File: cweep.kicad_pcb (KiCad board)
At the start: 2 copper layers, 106.6 x 82.7 mm, 51 parts

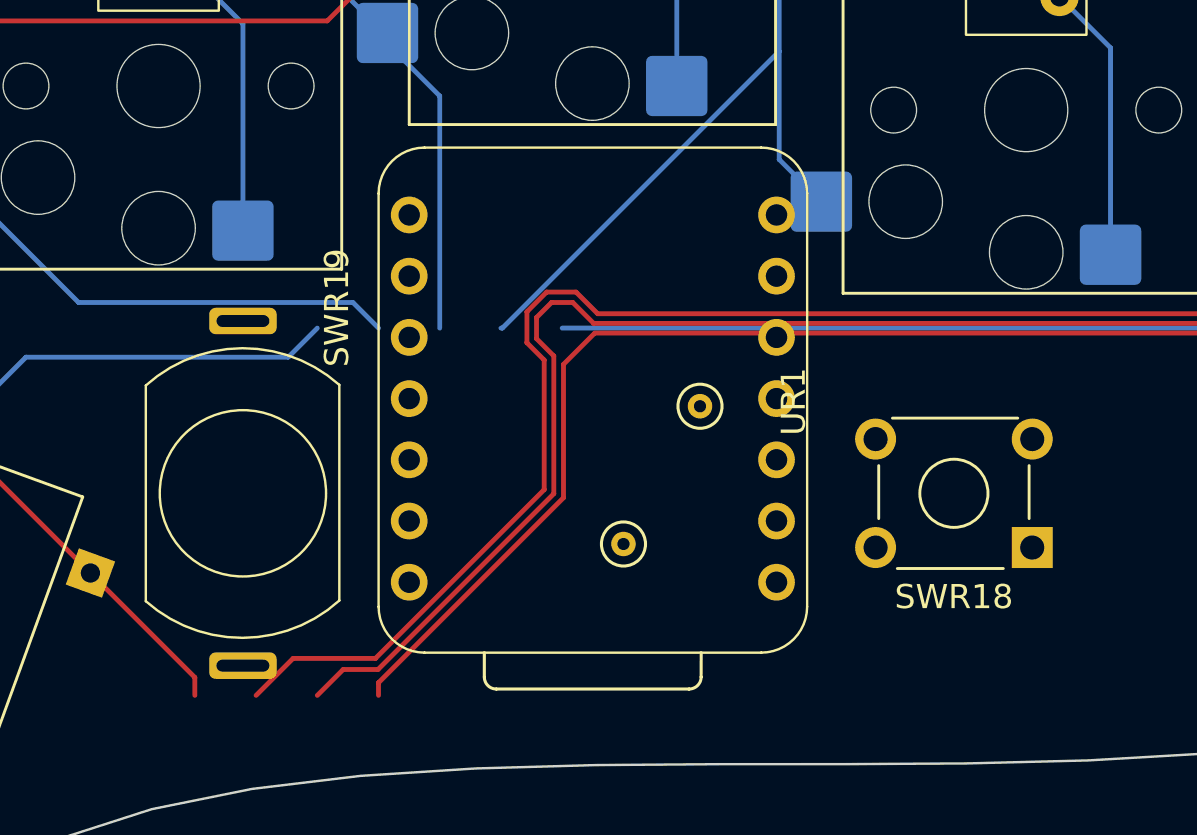
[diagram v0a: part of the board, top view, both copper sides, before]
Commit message: fix: align reset switch with power switch
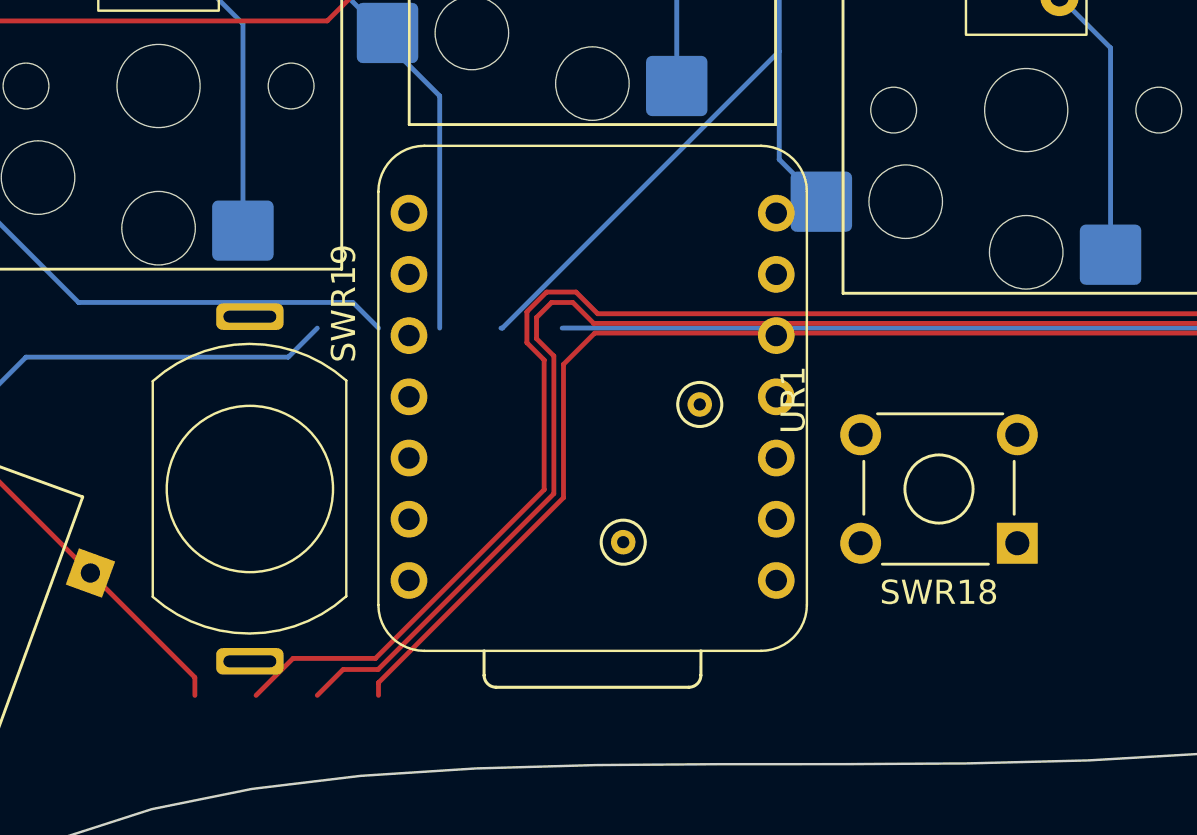
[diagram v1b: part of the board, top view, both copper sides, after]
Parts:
- moved SWR18 0.64 mm to (240.6, 102.0)
- moved SWR19 0.34 mm to (208.8, 99.7)
- moved UR1 0.07 mm to (222.9, 96.0)

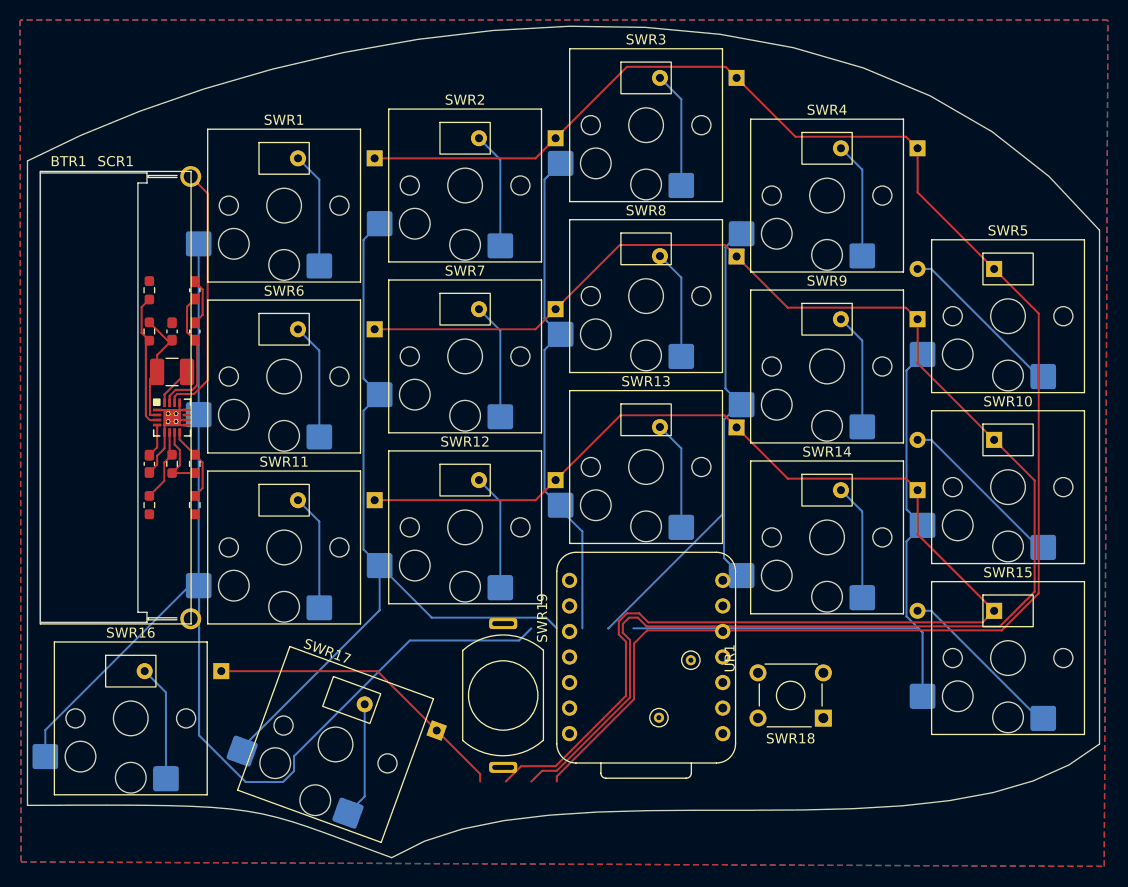
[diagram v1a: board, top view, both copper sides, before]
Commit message: fix: re-attach traces for gpio, power, and reset switches
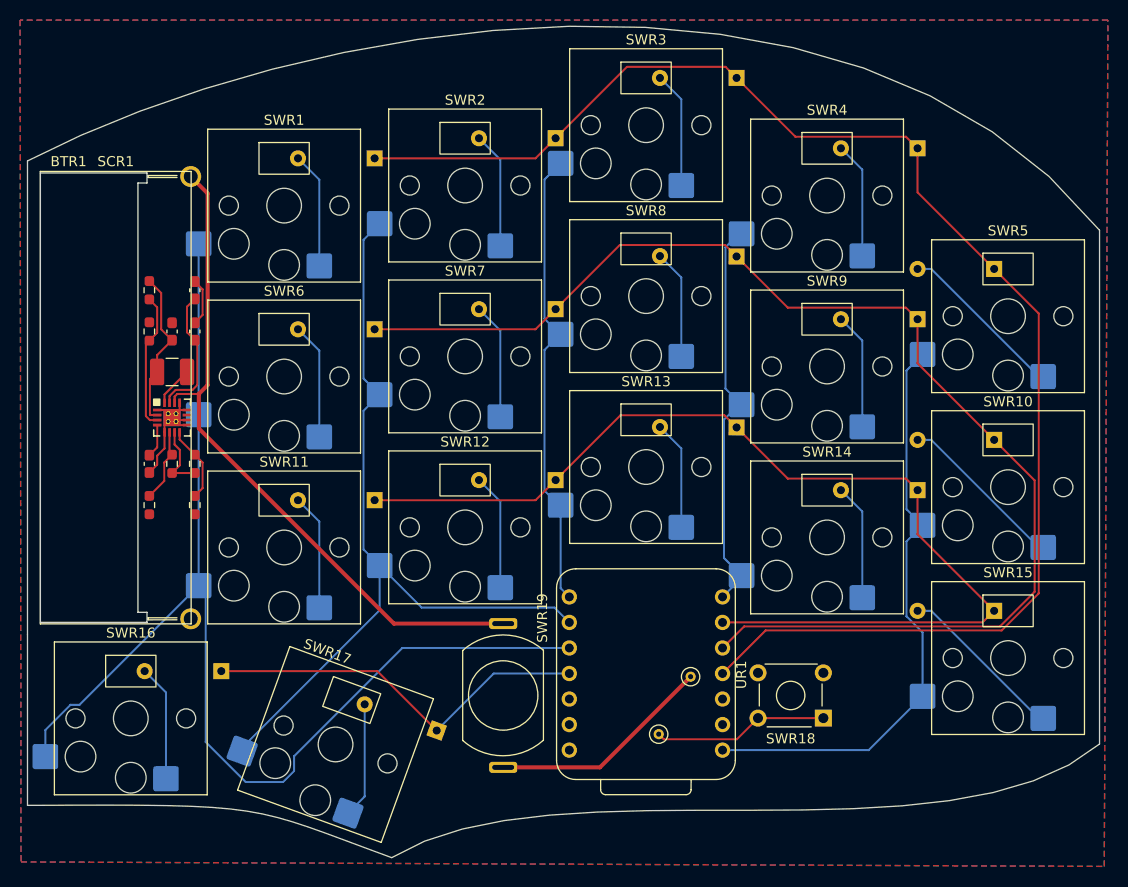
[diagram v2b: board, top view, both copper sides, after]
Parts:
- moved ROCR1 4.10 mm to (173.6, 63.5)
- moved ROCR2 4.10 mm to (173.6, 59.4)
- moved UR1 1.64 mm to (222.9, 97.7)
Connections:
- UR1 pad 10: /row r1 -> /column r0
- UR1 pad 11: /row r0 -> /row r3
- UR1 pad 2: /column r3 -> unconnected-(UR1-P0.03_A1_D1-Pad2)
- UR1 pad 3: /column r2 -> unconnected-(UR1-P0.28_A2_D2-Pad3)
- UR1 pad 4: /column r1 -> /row r0
- UR1 pad 5: /column r0 -> /row r1
- UR1 pad 6: unconnected-(UR1-P0.05_A5_D5_SCL-Pad6) -> /row r2
- UR1 pad 7: unconnected-(UR1-P1.11_D6_TX-Pad7) -> /column r3
- UR1 pad 8: /row r3 -> /column r2
- UR1 pad 9: /row r2 -> /column r1
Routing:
- net /VBATR: track 25.5 -> 67.6 mm
- net /row r2: track 137.4 -> 103.2 mm
- net /row r1: track 156.7 -> 126.2 mm
- net /row r0: track 170.0 -> 145.5 mm
- net Net-(SWR19-A): track 0.00 -> 22.4 mm
- net Net-(UR1-RESET): track 0.00 -> 17.5 mm
- net /column r3: track 53.4 -> 40.0 mm
- net /row r3: track 30.7 -> 39.4 mm
- net /column r4: track 65.6 -> 58.8 mm
- net /column r0: track 114.9 -> 118.8 mm
- net Net-(SCR1-+): track 12.0 -> 15.9 mm
- net /column r2: track 49.9 -> 46.2 mm
- net /column r1: track 81.0 -> 82.0 mm

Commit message: refactor: improve traces routing
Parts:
- turned UR1 to 0 degrees
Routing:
- net /column r0: track 118.8 -> 98.0 mm
- net /column r1: track 82.0 -> 100.3 mm

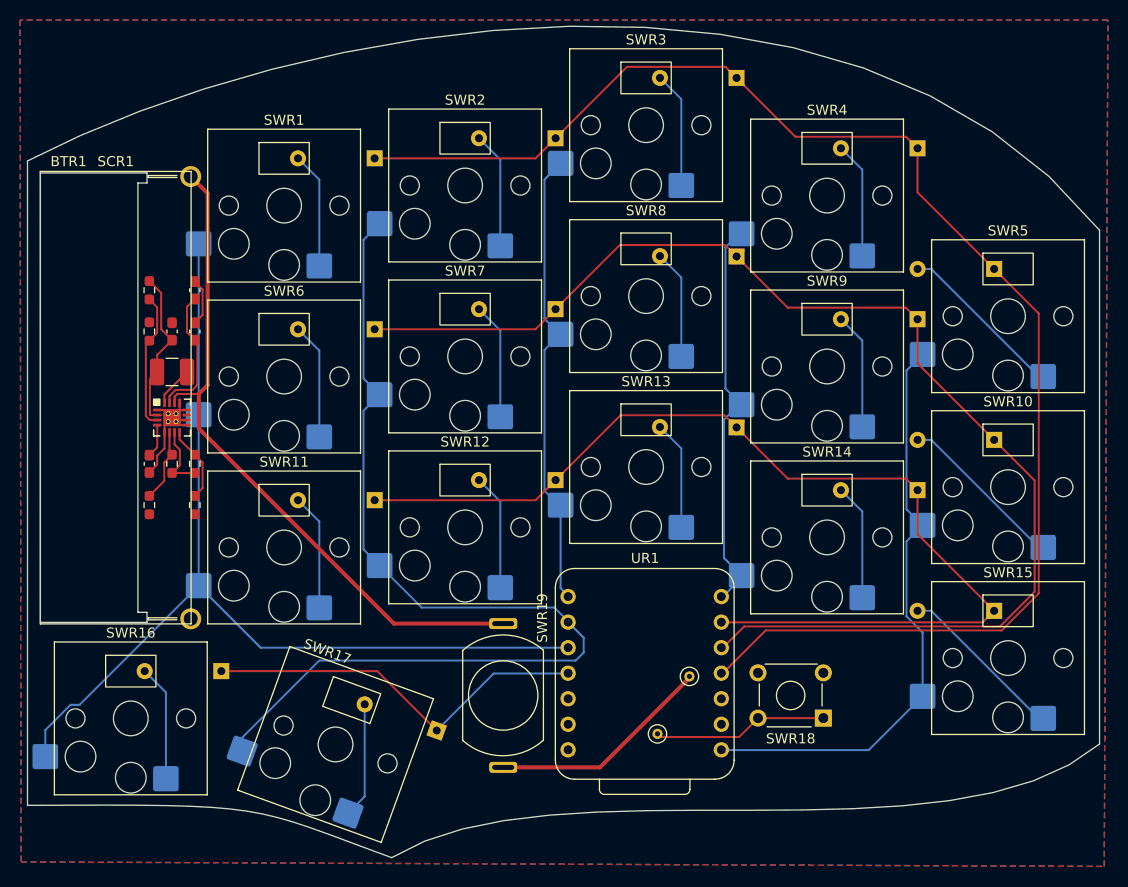
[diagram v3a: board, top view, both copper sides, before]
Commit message: fix: minor footprint and label alignments
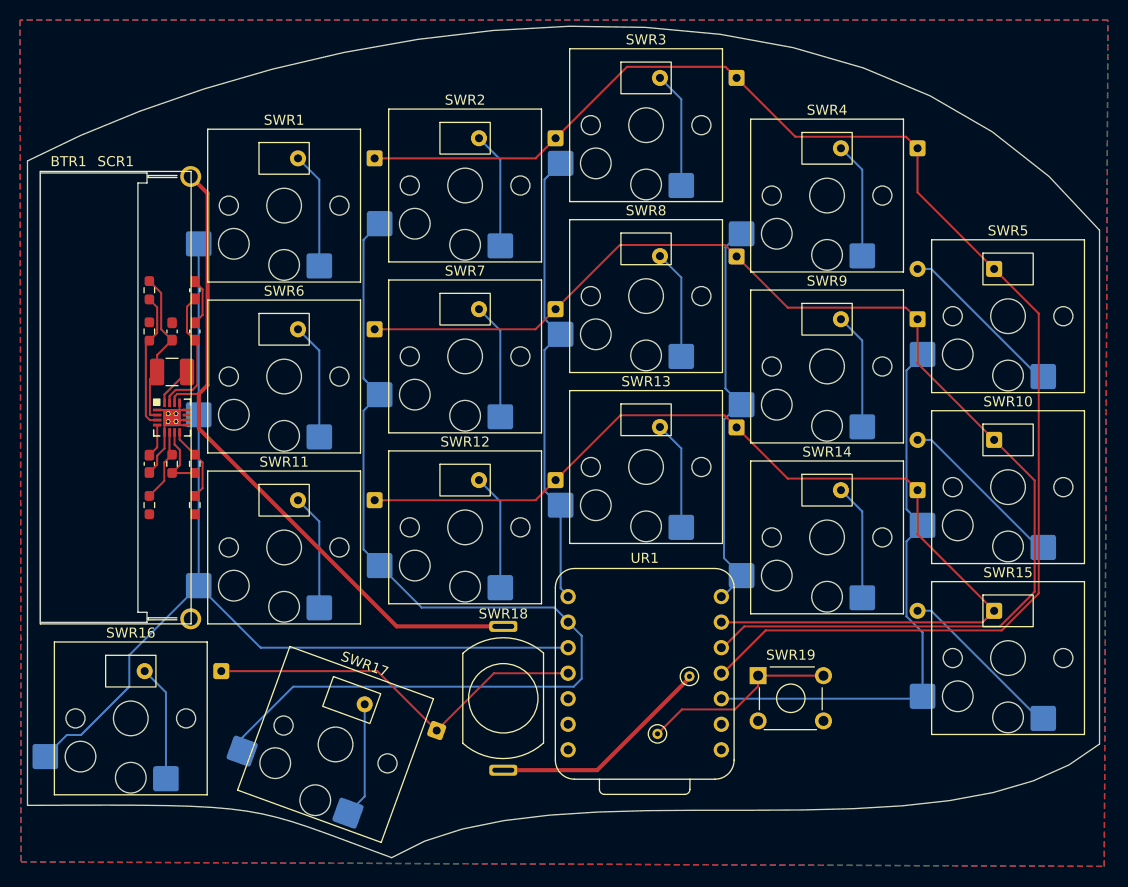
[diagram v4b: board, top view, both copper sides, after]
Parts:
- SWR18: value SW_Omron_B3FS -> SW_SPST; footprint Button_Switch_THT:SW_TH_Tactile_Omron_B3F-10xx -> KAN-15:SW_KAN-15_PHT
- SWR19: value SW_SPST -> SW_Omron_B3FS; footprint KAN-15:SW_KAN-15_PHT -> Button_Switch_THT:SW_TH_Tactile_Omron_B3F-10xx
- moved SWR18 31.9 mm to (208.8, 100.0), turned to 0 degrees
- moved SWR19 25.4 mm to (234.1, 97.7), turned to 0 degrees
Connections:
- SWR18 pad 1: Net-(UR1-RESET) -> Net-(SWR18-A)
- SWR18 pad 2: GND -> /VBATR
- SWR19 pad 1: Net-(SWR19-A) -> Net-(UR1-RESET)
- SWR19 pad 2: /VBATR -> GND
- UR1 pad 1: /column r4 -> unconnected-(UR1-P0.02_A0_D0-Pad1)
- UR1 pad 15: Net-(SWR19-A) -> Net-(SWR18-A)
- UR1 pad 3: unconnected-(UR1-P0.28_A2_D2-Pad3) -> /column r4
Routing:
- net Net-(SWR18-A): track 0.00 -> 22.5 mm
- net Net-(SWR19-A): track 22.4 -> 0.00 mm
- net Net-(UR1-RESET): track 17.3 -> 19.5 mm
- net /column r4: track 58.8 -> 56.8 mm
- net /column r1: track 100.3 -> 101.6 mm

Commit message: feat: add case mounting holes
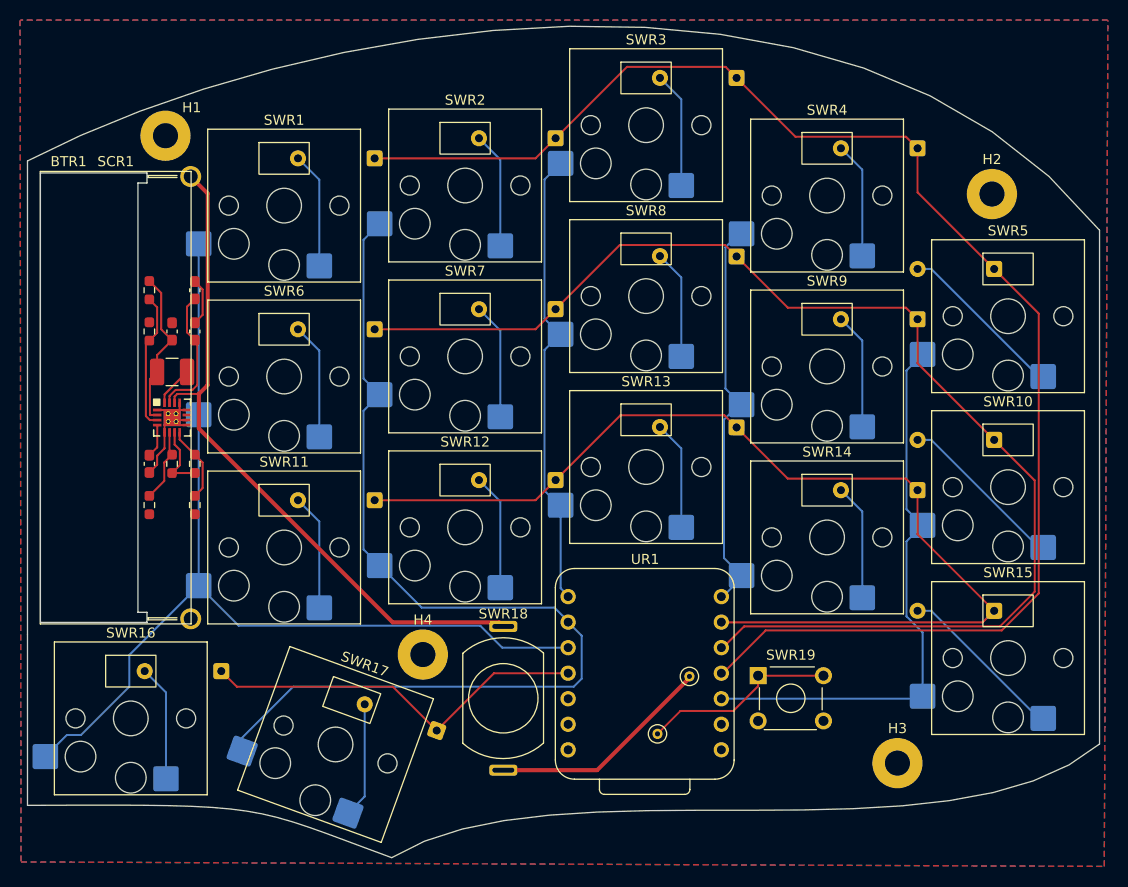
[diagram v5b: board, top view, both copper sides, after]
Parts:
- added H1: MountingHole_Pad, MountingHole:MountingHole_2.5mm_Pad, F.Cu at (175.2, 44.0)
- added H2: MountingHole_Pad, MountingHole:MountingHole_2.5mm_Pad, F.Cu at (257.4, 49.9)
- added H3: MountingHole_Pad, MountingHole:MountingHole_2.5mm_Pad, F.Cu at (248.0, 106.5)
- added H4: MountingHole_Pad, MountingHole:MountingHole_2.5mm_Pad, F.Cu at (200.8, 95.7)
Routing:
- net /column r0: track 98.3 -> 97.4 mm

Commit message: feat: 2.5mm -> 2.2mm mounting holes
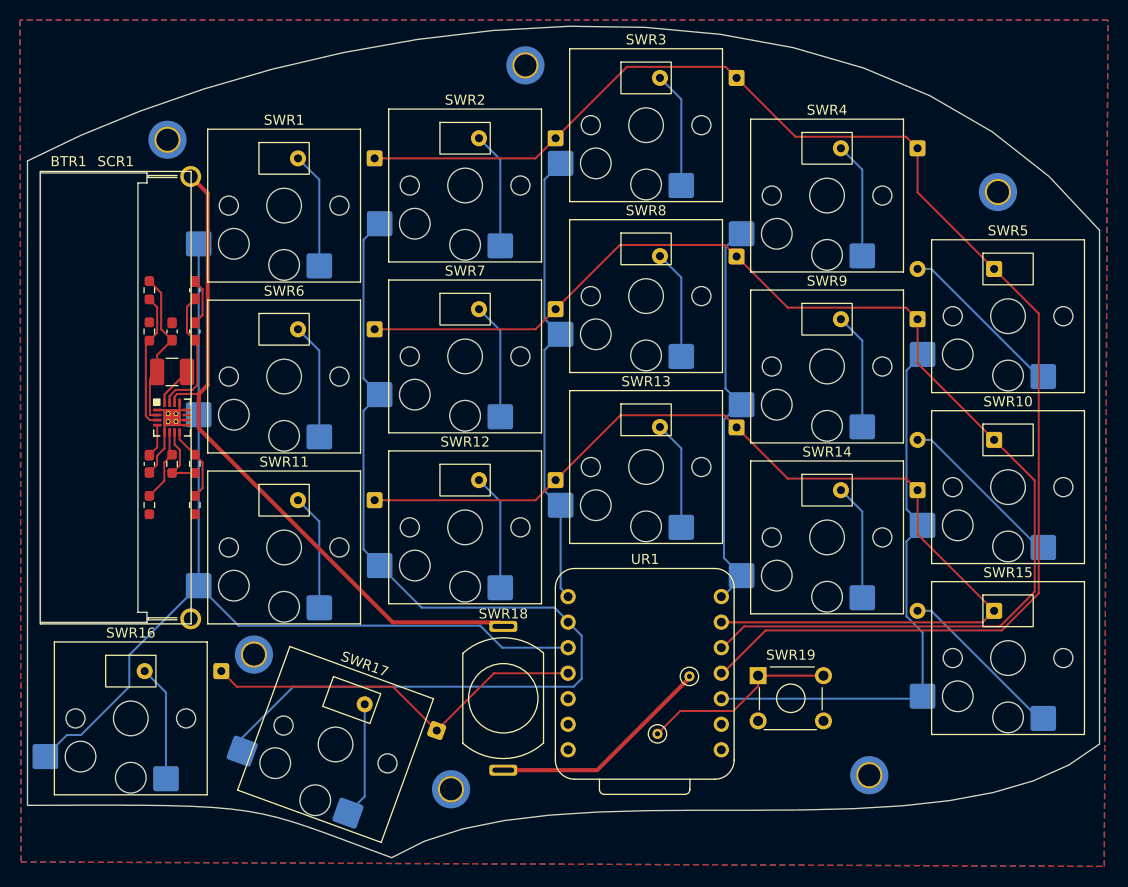
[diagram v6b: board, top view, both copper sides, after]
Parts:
- added H5: MountingHole_Pad, MountingHole:MountingHole_2.2mm_M2_DIN965_Pad_TopOnly, B.Cu at (175.4, 44.5)
- added H6: MountingHole_Pad, MountingHole:MountingHole_2.2mm_M2_DIN965_Pad_TopOnly, B.Cu at (211.0, 37.0)
- H1, H2, H3, H4: footprint MountingHole:MountingHole_2.5mm_Pad -> MountingHole:MountingHole_2.2mm_M2_DIN965_Pad_TopOnly; moved to B.Cu
- moved H1 83.0 mm to (258.0, 49.6), turned to 180 degrees
- moved H2 59.1 mm to (245.2, 107.7), turned to 180 degrees
- moved H3 44.5 mm to (203.6, 109.0), turned to 180 degrees
- moved H4 16.8 mm to (184.0, 95.7), turned to 180 degrees
